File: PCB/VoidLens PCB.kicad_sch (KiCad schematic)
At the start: 73 parts, among them IC1 BMI270, J1 solder pad, J2 JST-XH-2 Pin, J3 USB4105-GF-A, J4 JST_XH for led Strip, J5 Programming_Pins, J6 power jumper, Q1 MMBT3904-E, Q2 DXT2011P5-13, SW1 SW_SPST, SW2 SW_Push, SW3 SW_SPDT, SW4 SW_Push, U1 BQ24074RGT, U2 ATmega32U4-A, U3 NRF24L01, U5 TPS61022, U6 TPS27081ADDCR, Y1 16Mhz, Y2 16mhz

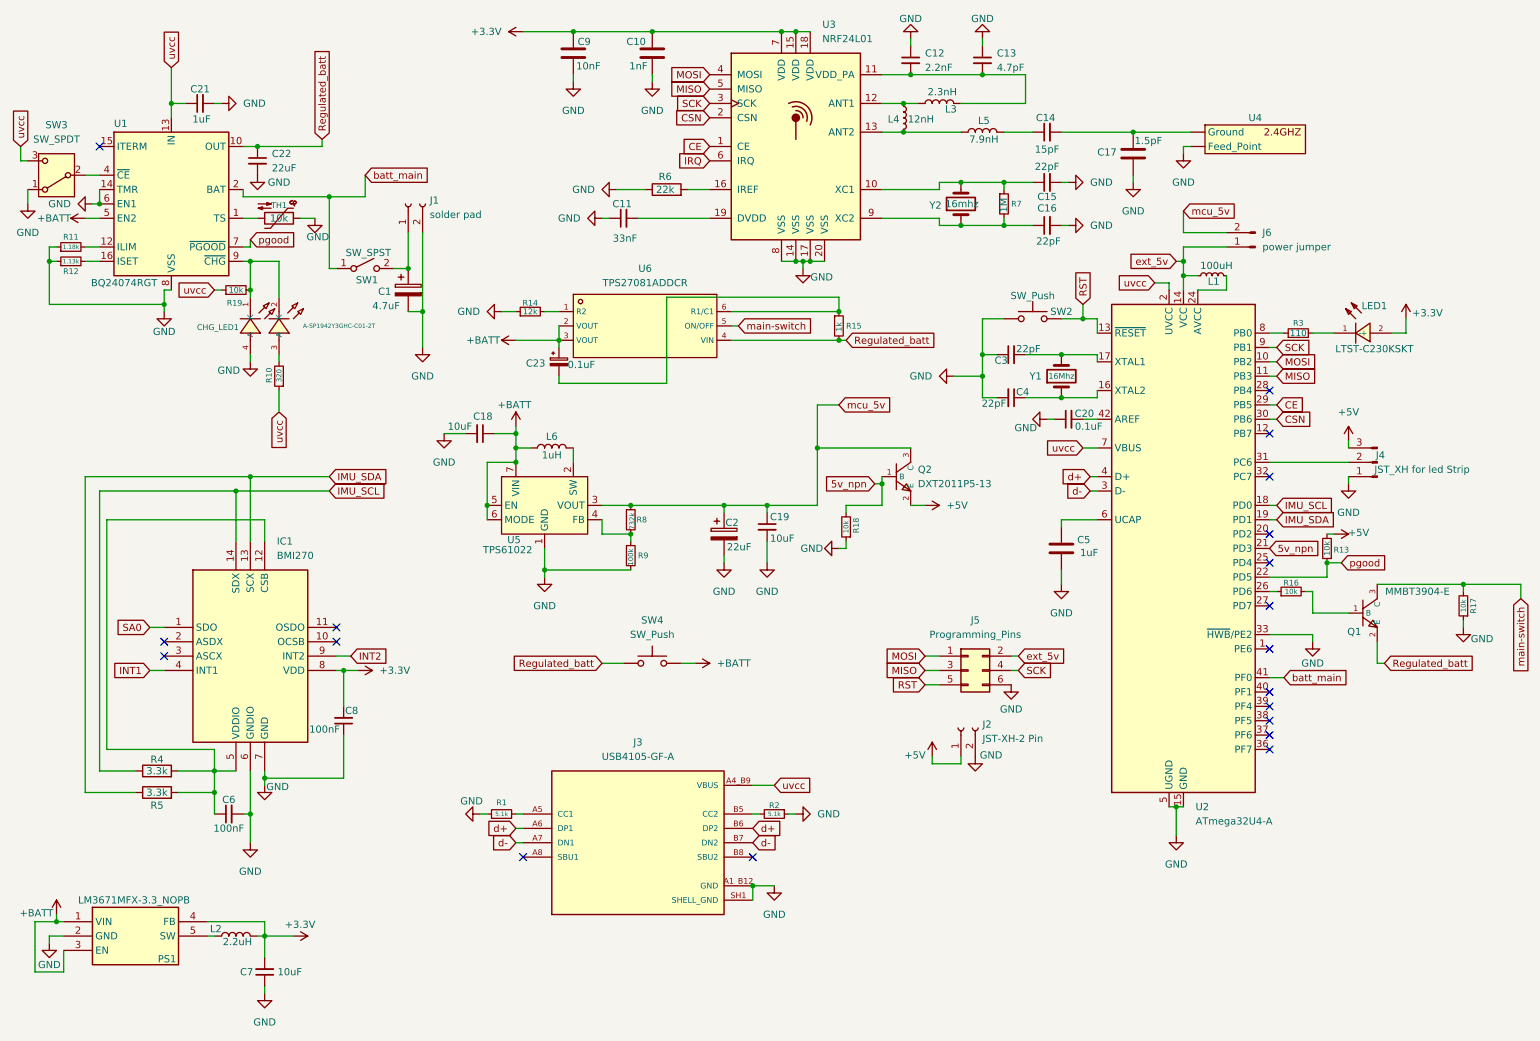
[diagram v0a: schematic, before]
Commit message: finished assigning and imported to pcb editor
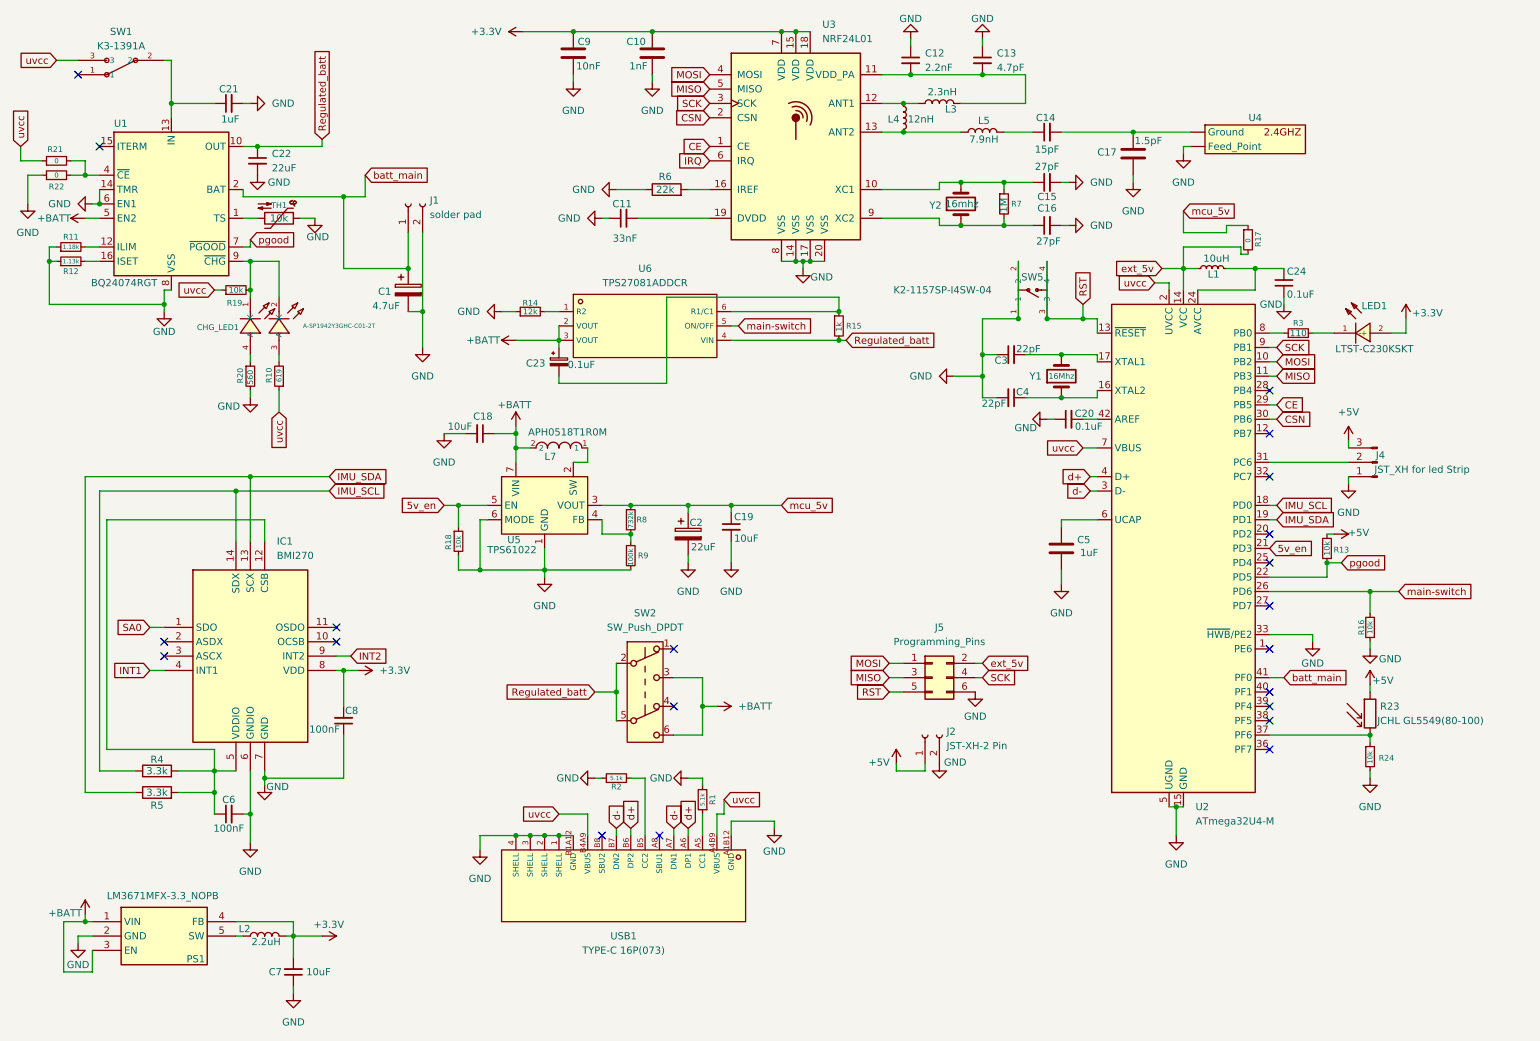
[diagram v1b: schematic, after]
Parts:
- removed J3: USB4105-GF-A, USB4105-GF-A:GCT_USB4105-GF-A, symbol Kicad_sym:USB4105-GF-A
- removed J6: power jumper, symbol Connector:Conn_01x02_Pin
- removed L6: 1uH, symbol Device:L
- removed Q1: MMBT3904-E, lcsc_footprints:C41371422_SOT-23-3_L2_9-W1_4-P1_90-LS2_5-BR, symbol lcsc_imported:MMBT3904-E
- removed Q2: DXT2011P5-13, lcsc_footprints:C155259_POWERDI-5_L5_4-W4_0-LS6_5-RD, symbol lcsc_imported:DXT2011P5-13
- removed SW1: SW_SPST, symbol Switch:SW_SPST
- removed SW2, SW4: SW_Push, symbol Switch:SW_Push
- removed SW3: SW_SPDT, symbol Switch:SW_SPDT
- removed U2: ATmega32U4-A, Package_QFP:TQFP-44_10x10mm_P0.8mm, symbol MCU_Microchip_ATmega:ATmega32U4-A
- added C24: 0.1uF, Capacitor_SMD:C_0603_1608Metric_Pad1.08x0.95mm_HandSolder, symbol Device:C_Small
- added L7: APH0518T1R0M, lcsc_footprints:C5349672_IND-SMD_L5_4-W5_2, symbol lcsc_imported:APH0518T1R0M
- added R20: 560, Resistor_SMD:R_0603_1608Metric_Pad0.98x0.95mm_HandSolder, symbol Device:R_Small
- added R21, R22: 0, Resistor_SMD:R_0603_1608Metric_Pad0.98x0.95mm_HandSolder, symbol Device:R_Small
- added R23: JCHL GL5549(80-100), OptoDevice:R_LDR_4.9x4.2mm_P2.54mm_Vertical, symbol Device:R_Photo
- added R24: 10k, Resistor_SMD:R_0603_1608Metric_Pad0.98x0.95mm_HandSolder, symbol Device:R_Small
- added SW1: K3-1391A, lcsc_footprints:C92655_SW-TH_K3-1391A, symbol lcsc_imported:K3-1391A
- added SW2: SW_Push_DPDT, Kicad:SW-TH_6P-L5.8-W5.8-P2.00-LS4.5-BL, symbol Switch:SW_Push_DPDT
- added SW5: K2-1157SP-I4SW-04, lcsc_footprints:C2909692_SW-SMD_4P-L6_2-W6_2-P4_50-LS8_6, symbol lcsc_imported:K2-1157SP-I4SW-04
- added U2: ATmega32U4-M, Package_DFN_QFN:QFN-44-1EP_7x7mm_P0.5mm_EP5.2x5.2mm, symbol MCU_Microchip_ATmega:ATmega32U4-M
- added USB1: TYPE-C 16P(073), lcsc_footprints:C668624_USB-C-SMD_TYPE-C16PIN_C668624, symbol lcsc_imported:TYPE-C_16P(073)
- C15, C16: value 22pF -> 27pF
- J4: footprint (none) -> Connector_JST:JST_XH_B3B-XH-A_1x03_P2.50mm_Vertical
- J5: footprint (none) -> Connector_PinHeader_2.54mm:PinHeader_2x03_P2.54mm_Vertical
- L1: value 100uH -> 10uH; footprint (none) -> Inductor_SMD:L_0805_2012Metric_Pad1.05x1.20mm_HandSolder
- L2: footprint (none) -> Inductor_SMD:L_1008_2520Metric_Pad1.43x2.20mm_HandSolder
- L3: footprint (none) -> Inductor_SMD:L_0201_0603Metric_Pad0.64x0.40mm_HandSolder
- L4, L5: footprint (none) -> Inductor_SMD:L_0402_1005Metric_Pad0.77x0.64mm_HandSolder
- PS1: footprint (none) -> Package_TO_SOT_SMD:SOT-23-5_HandSoldering
- R1, R11, R12, R13, R14, R15, R16, R18, R19, R2, R3, R4, R5, R6, R7, R8, R9: footprint (none) -> Resistor_SMD:R_0603_1608Metric_Pad0.98x0.95mm_HandSolder
- R10: value 320 -> 619; footprint (none) -> Resistor_SMD:R_0603_1608Metric_Pad0.98x0.95mm_HandSolder
- R17: value 10k -> 0; footprint (none) -> Resistor_SMD:R_0603_1608Metric_Pad0.98x0.95mm_HandSolder
- TH1: footprint (none) -> Resistor_THT:R_Axial_DIN0204_L3.6mm_D1.6mm_P5.08mm_Horizontal
- U4: value ~ -> (none); footprint (none) -> Kicad:2.4Ghz PCB Antenna
- Y1, Y2: footprint (none) -> Crystal:Crystal_HC49-4H_Vertical
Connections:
- net 5v_npn is gone; now on net GND: R18.2
- net +5V: now also R23.1
- net +BATT: now also L7.2, SW2.3 (C), SW2.6 (C); no longer U5.5 (EN), U5.6 (MODE)
- net CE: now also U2.29 (PB5)
- net CSN: now also U2.30 (PB6)
- net GND: now also R1.2, R16.1, U5.6 (MODE), C24.2, R20.2, R22.1, R24.2, SW5.1, SW5.2, U2.15 (GND), U2.23 (GND), U2.33 (~{HWB}/PE2), U2.35 (GND), U2.43 (GND), U2.45 (GND), U2.5 (UGND), USB1.1 (SHELL), USB1.2 (SHELL), USB1.3 (SHELL), USB1.4 (SHELL), USB1.A1B12 (GND), USB1.B1A12 (GND); no longer CHG_LED1.4 (A), R1.1, R17.1, R18.1
- net IMU_SCL: now also U2.18 (PD0)
- net IMU_SDA: now also U2.19 (PD1)
- net MISO: now also U2.11 (PB3)
- net MOSI: now also U2.10 (PB2)
- net RST: now also SW5.3, SW5.4, U2.13 (~{RESET})
- net Regulated_batt: now also SW2.2 (B), SW2.5 (B)
- net SCK: now also U2.9 (PB1)
- net batt_main: now also C1.1, J1.1 (Pin_1), U2.41 (PF0)
- net d+: now also U2.4 (D+), USB1.A6 (DP1), USB1.B6 (DP2)
- net d-: now also U2.3 (D-), USB1.A7 (DN1), USB1.B7 (DN2)
- net ext_5v: now also R17.2, U2.14 (VCC), U2.34 (VCC)
- net main-switch: now also R16.2, U2.26 (PD6); no longer R17.2
- net mcu_5v: now also R17.1
- net pgood: now also U2.22 (PD5)
- net at C3.2, Y1.2: now also U2.17 (XTAL1)
- net at R2.2: now also USB1.B5 (CC2)
- net at C4.1, Y1.1: now also U2.16 (XTAL2)
- net at L1.2: now also C24.1, U2.24 (AVCC), U2.44 (AVCC)
- net at J4.2 (Pin_2): now also U2.31 (PC6)
- net at C20.2: now also U2.42 (AREF)
- net at C5.1: now also U2.6 (UCAP)
- net at R3.1: now also U2.8 (PB0)
- net at U5.2 (SW): now also L7.1
- net at U1.4 (~{CE}): now also R21.2, R22.2
- net VBUS: no longer names the net of C21.1, U1.13 (IN)
- net VBUS: now also SW1.2; no longer R10.1, R19.1
- new net: R23.2, R24.1, U2.37 (PF6)
- new net: R1.1, USB1.A5 (CC1)
- new net: CHG_LED1.4 (A), R20.1
- new net 5v_en: R18.1, U2.21 (PD3), U5.5 (EN)
- new net uvcc: R10.1, R19.1, R21.1, SW1.3, U2.2 (UVCC), U2.7 (VBUS), USB1.A4B9 (VBUS), USB1.B4A9 (VBUS)
- no-connect marks 19 -> 21
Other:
- moved on the sheet: C19, C2, C21, C7, J2, J5, L1, L2, PS1

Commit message: Arrangeed components to their positions in pcb
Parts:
- C22: footprint Capacitor_SMD:C_0603_1608Metric_Pad1.08x0.95mm_HandSolder -> Capacitor_SMD:CP_Elec_4x5.4
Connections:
- net batt_main: now also SW1.2; no longer C1.1, J1.1 (Pin_1)
- net uvcc: now also C21.1, U1.13 (IN); no longer SW1.3
- net at SW1.1: now also C1.1, J1.1 (Pin_1)
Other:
- moved on the sheet: C1, J1

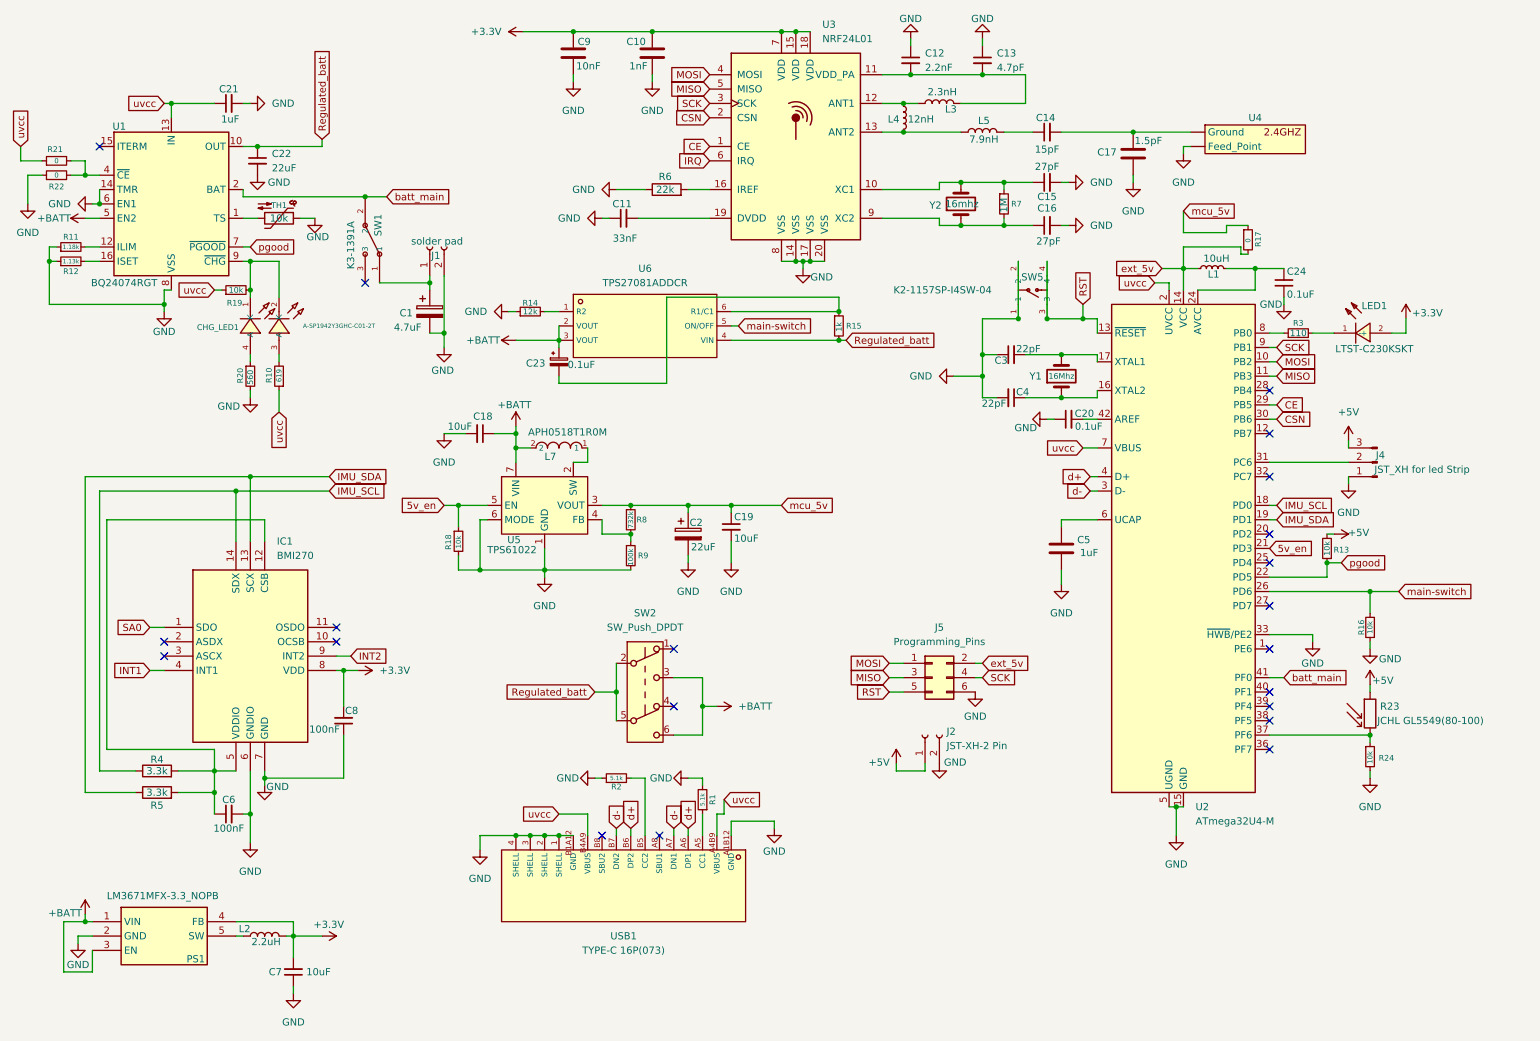
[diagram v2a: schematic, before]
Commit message: routed more components in the pcb
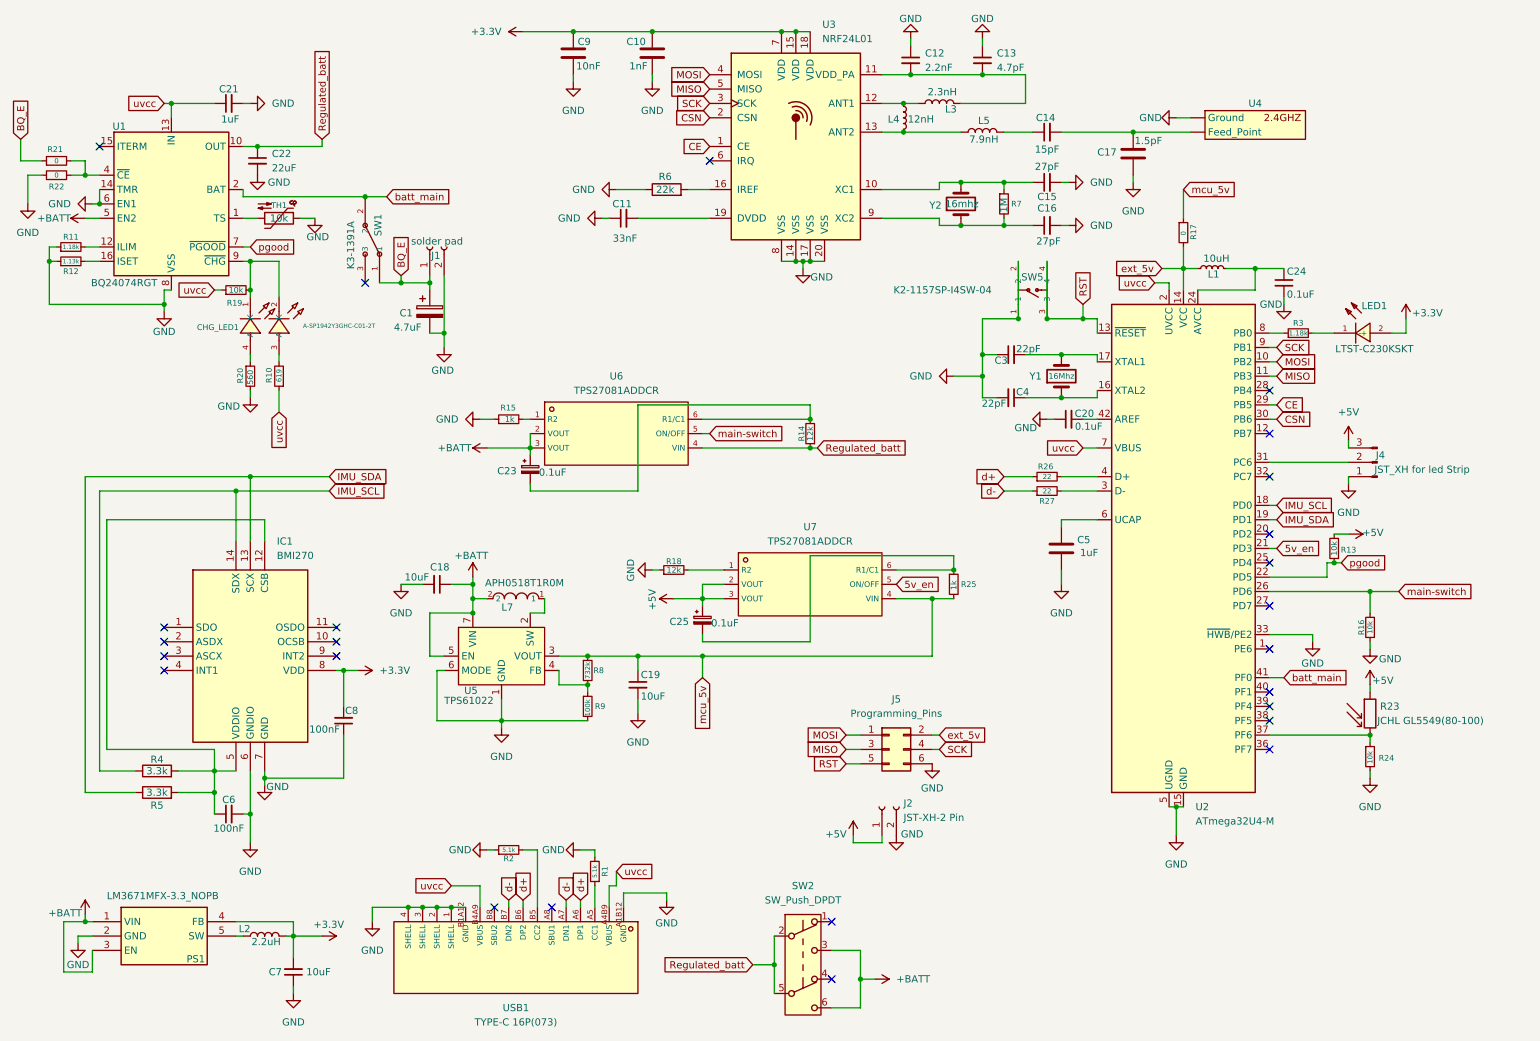
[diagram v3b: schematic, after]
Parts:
- removed C2: 22uF, Capacitor_SMD:CP_Elec_4x5.4, symbol Device:C_Polarized
- added C25: 0.1uF, Capacitor_SMD:C_0603_1608Metric_Pad1.08x0.95mm_HandSolder, symbol Device:C_Polarized_Small
- added R25: 1k, Resistor_SMD:R_0603_1608Metric_Pad0.98x0.95mm_HandSolder, symbol Device:R_Small
- added R26, R27: 22, Resistor_SMD:R_0603_1608Metric_Pad0.98x0.95mm_HandSolder, symbol Device:R_Small
- added U7: TPS27081ADDCR, lcsc_footprints:C128404_SOT-23-6_L2_9-W1_6-P0_95-LS2_8-BR, symbol lcsc_imported:TPS27081ADDCR
- R18: value 10k -> 12k
- R3: value 110 -> 1.18k
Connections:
- net +5V: now also C25.1, U7.2 (VOUT), U7.3 (VOUT)
- net +BATT: now also U5.5 (EN)
- net 5v_en: now also U7.5 (ON/OFF); no longer R18.1, U5.5 (EN)
- net GND: now also R15.1, R18.1; no longer R14.1, R18.2
- net Regulated_batt: now also R14.1; no longer R15.2
- net d+: now also R26.1; no longer U2.4 (D+)
- net d-: now also R27.1; no longer U2.3 (D-)
- net mcu_5v: now also R25.2, U7.4 (VIN)
- net uvcc: no longer R21.1
- net at U6.1 (R2): now also R15.2; no longer R14.2
- net at C23.2, U6.6 (R1/C1): now also R14.2; no longer R15.1
- net BQ_E: now reaches C1.1, J1.1 (Pin_1), SW1.1
- net BQ_E: now also R21.1
- net INT1: no longer names the net of IC1.4 (INT1)
- net INT2: no longer names the net of IC1.9 (INT2)
- net IRQ: no longer names the net of U3.6 (IRQ)
- net SA0: no longer names the net of IC1.1 (SDO)
- new net: R27.2, U2.3 (D-)
- new net: R26.2, U2.4 (D+)
- new net: R18.2, U7.1 (R2)
- new net: C25.2, R25.1, U7.6 (R1/C1)
- no-connect marks 21 -> 25
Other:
- moved on the sheet: C18, C19, C23, J2, J5, L7, R1, R13, R17, R2, R8, R9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
